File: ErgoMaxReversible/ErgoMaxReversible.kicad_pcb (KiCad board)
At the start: 2 copper layers, 182.8 x 169.2 mm, 104 parts, among them J1 PJ-320A, K1 KEYSW, K10 KEYSW, K11 KEYSW, K12 KEYSW, K13 KEYSW, K14 KEYSW, K15 KEYSW, K16 KEYSW, K17 KEYSW, K18 KEYSW, K19 KEYSW, K2 KEYSW, K20 KEYSW, K21 KEYSW, K22 KEYSW, K23 KEYSW, K24 KEYSW, K25 KEYSW, K26 KEYSW, K27 KEYSW, K28 KEYSW, K29 KEYSW, K3 KEYSW, K30 KEYSW, K31 KEYSW, K32 KEYSW, K33 KEYSW, K34 KEYSW, K35 KEYSW, K36 KEYSW, K37 KEYSW, K38 KEYSW, K39 KEYSW, K4 KEYSW, K40 KEYSW, K41 KEYSW, K42 KEYSW, K43 KEYSW, K44 KEYSW, K5 KEYSW, K6 KEYSW, K7 KEYSW, K8 KEYSW, K9 KEYSW, U1 ProMicro

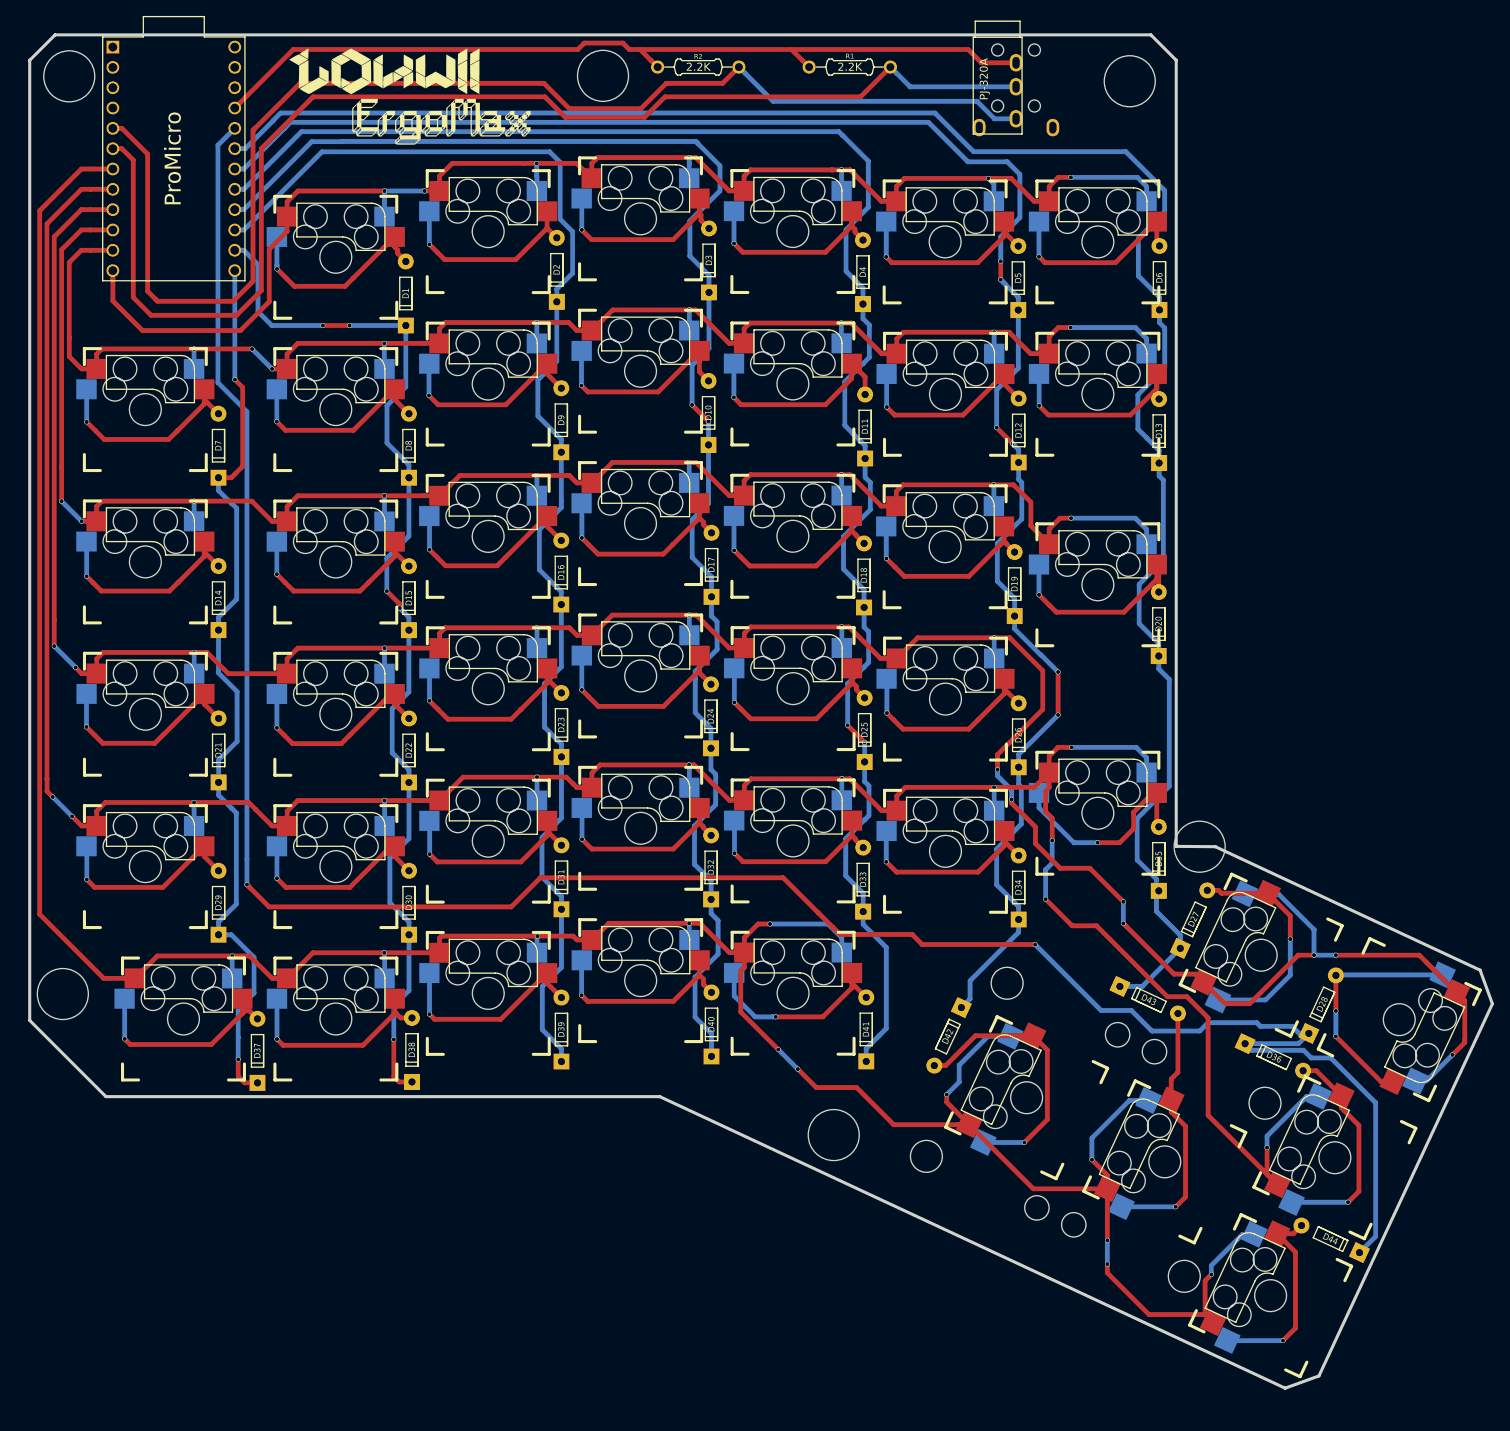
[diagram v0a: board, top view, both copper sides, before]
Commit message: improve footprints on reversible PCB and add sides markings
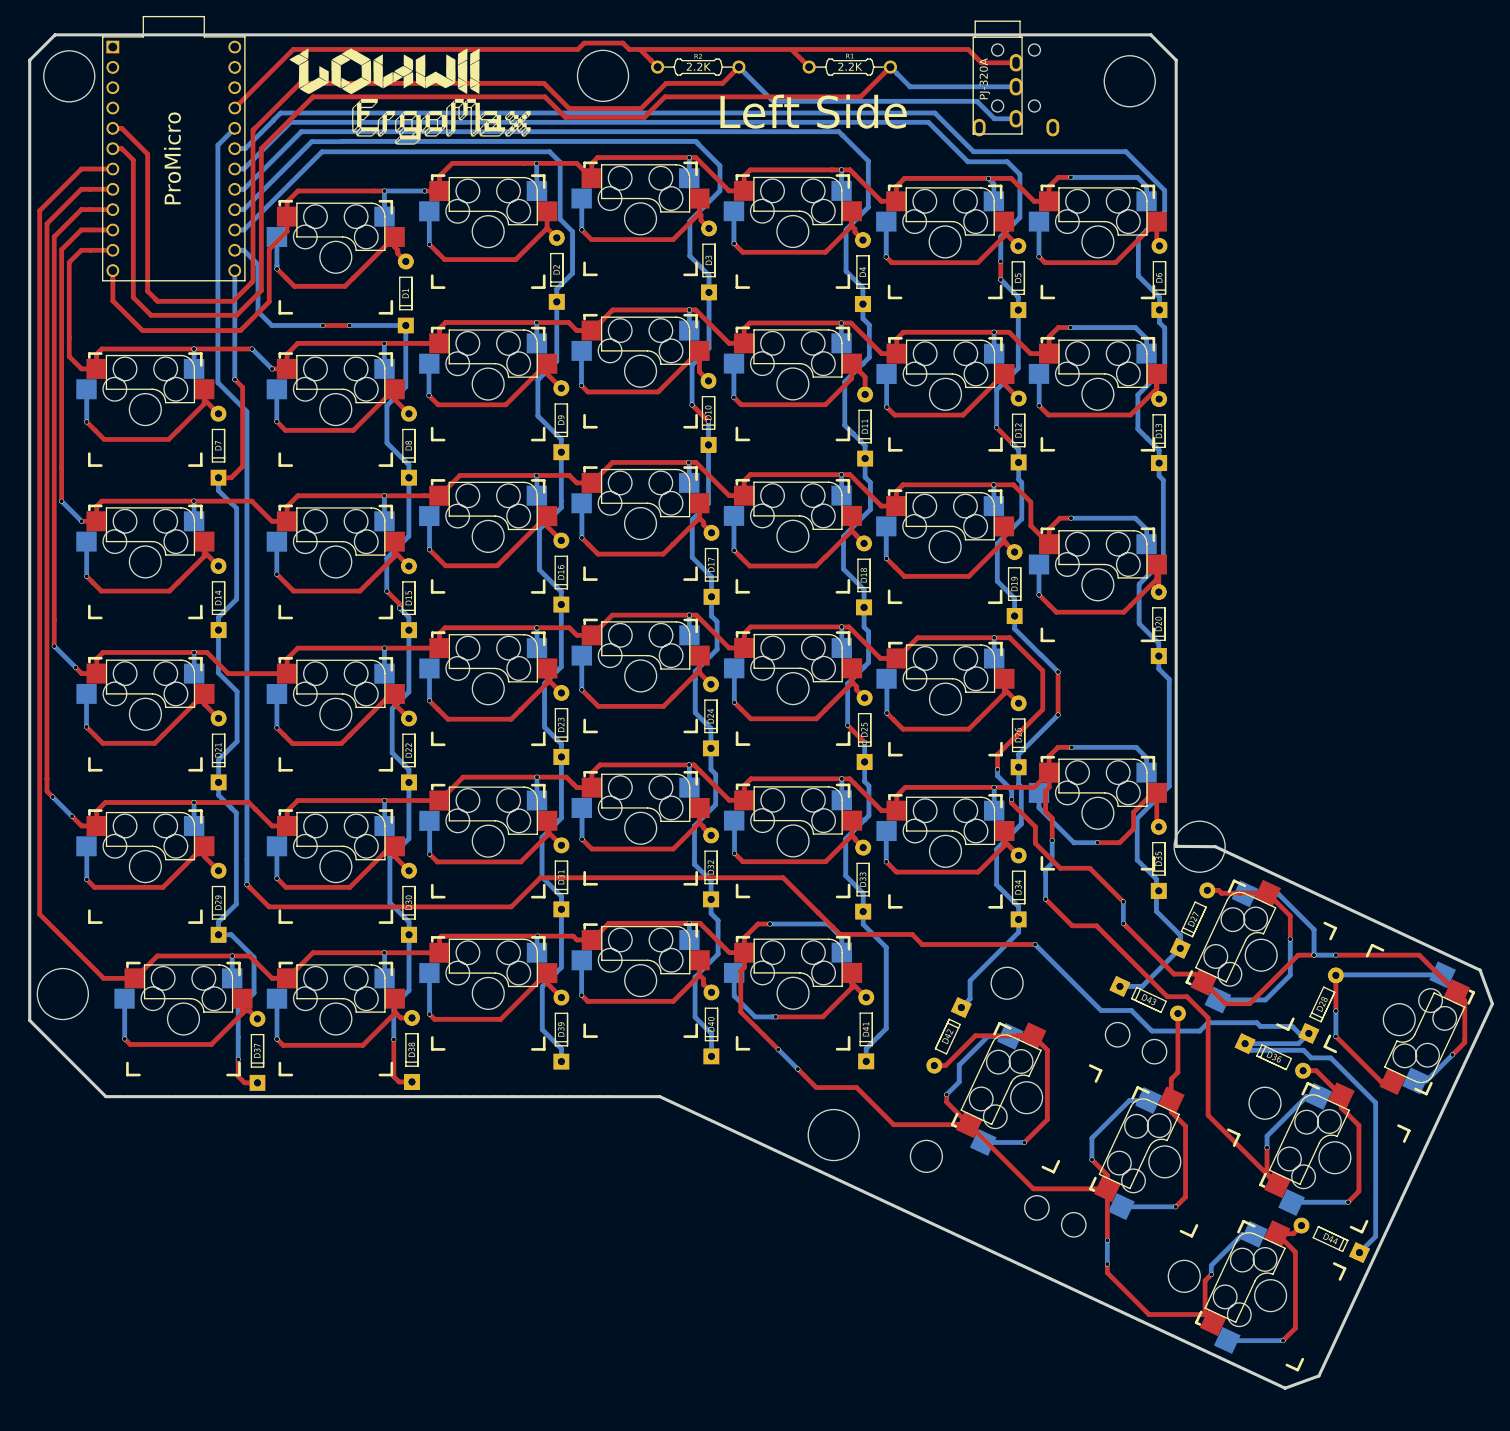
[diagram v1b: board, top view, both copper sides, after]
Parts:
- added Lg5: Logo, ErgoMax:LeftSideText, F.Cu at (208.2, 45.7)
- added Lg6: Logo, ErgoMax:RightSideText, F.Cu at (208.2, 45.7)
- K1, K10, K11, K12, K13, K14, K15, K16, K17, K18, K19, K2, K20, K21, K22, K23, K24, K25, K26, K27, K28, K29, K3, K30, K31, K32, K33, K34, K35, K36, K37, K38, K39, K4, K40, K41, K42, K43, K44, K5, K6, K7, K8, K9: footprint keyboard_parts:Kailh_MX_Socket_reversible -> ErgoMax:Kailh_MX_Socket_reversible

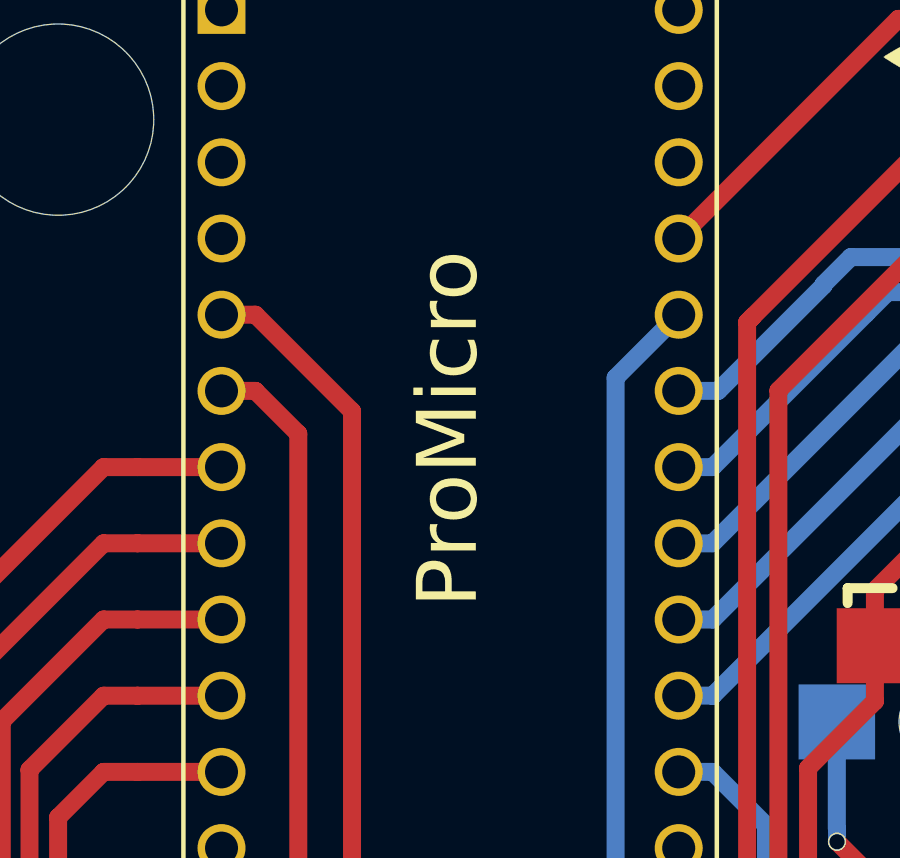
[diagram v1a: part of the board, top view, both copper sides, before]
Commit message: add readme for reversible PCB
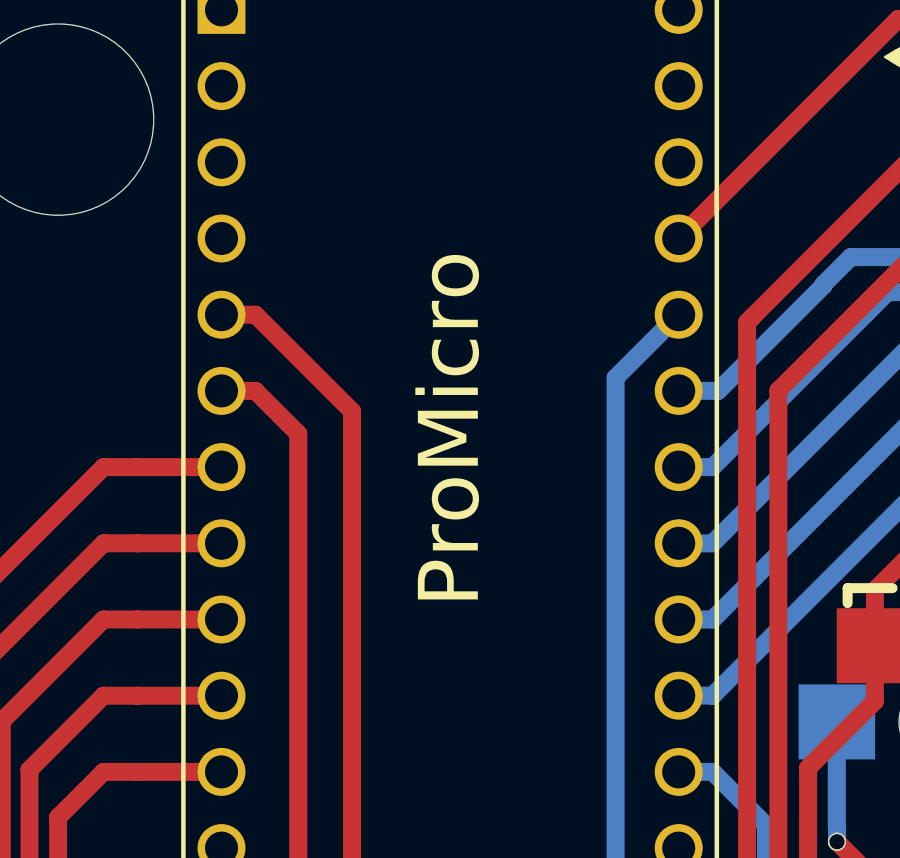
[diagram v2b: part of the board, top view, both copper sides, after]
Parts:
- U1: footprint promicro:ProMicro -> ErgoMax:ProMicroReversible

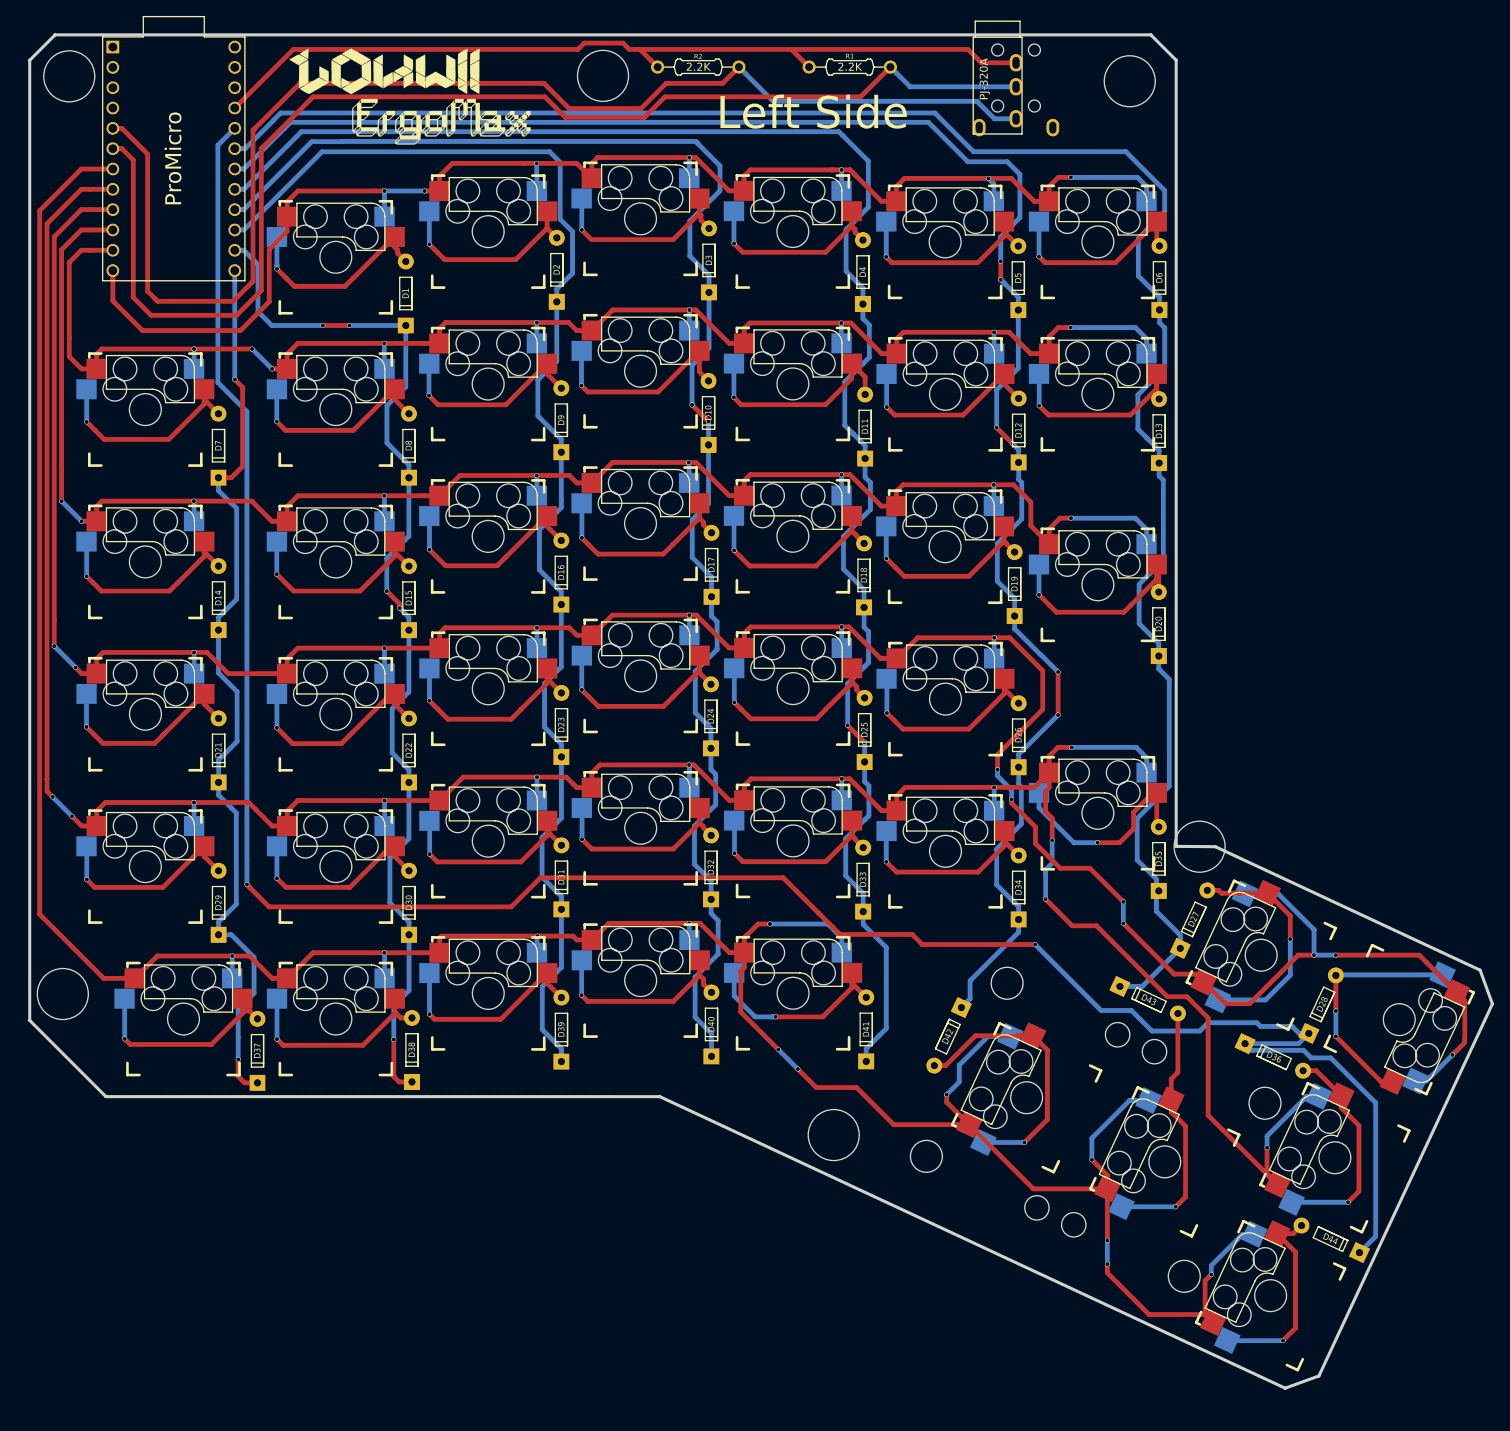
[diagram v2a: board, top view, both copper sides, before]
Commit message: Fix ground plane on reversible PCB
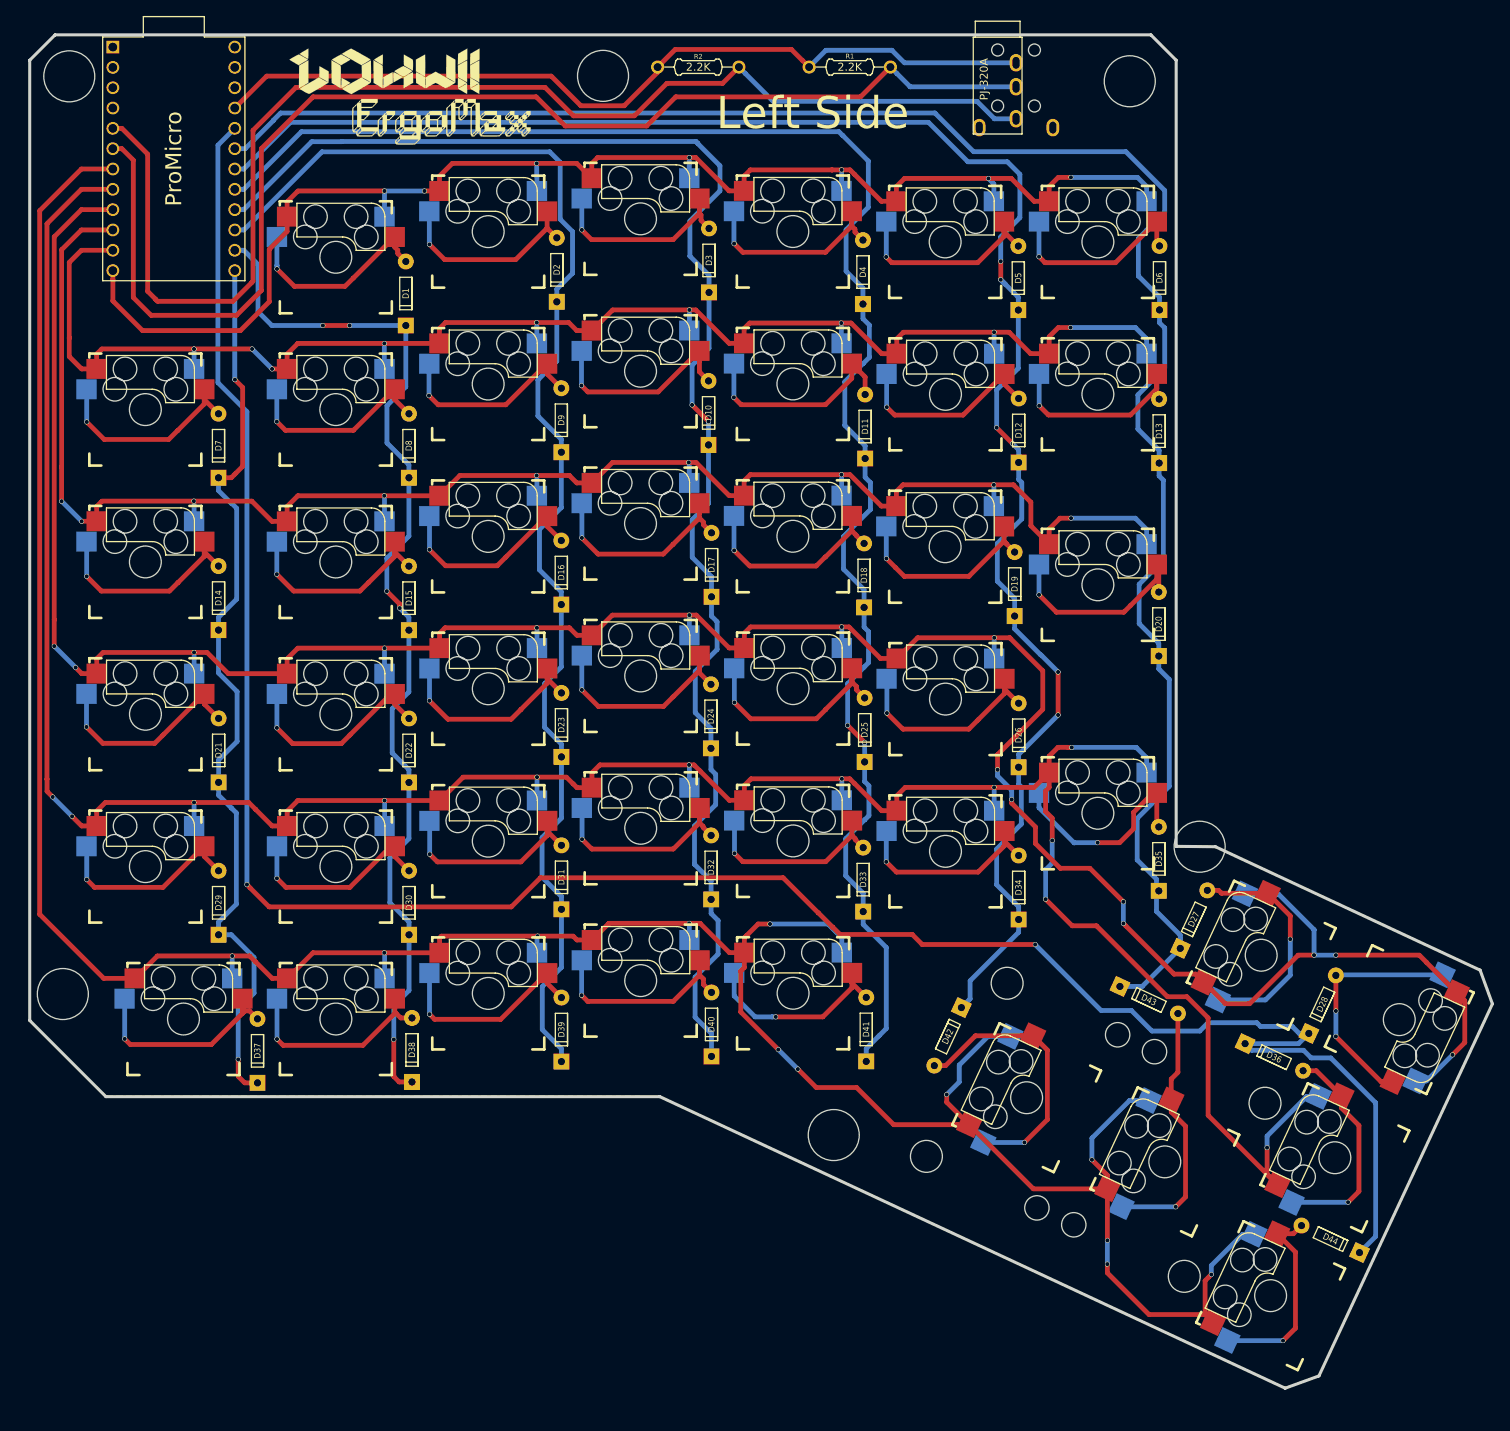
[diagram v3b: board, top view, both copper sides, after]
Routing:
- net Net-(D3-Pad2): track 28.0 -> 26.0 mm
- net Net-(D42-Pad2): track 36.2 -> 34.3 mm
- net Net-(D4-Pad2): track 27.9 -> 26.0 mm
- net VCC: track 108.3 -> 106.6 mm
- net Net-(D36-Pad2): track 29.0 -> 27.9 mm
- net SCL: track 158.0 -> 158.9 mm
- net Net-(D44-Pad2): track 26.3 -> 25.4 mm
- net /Col7: track 289.2 -> 288.7 mm
- net /Col6: track 239.1 -> 238.5 mm
- net Net-(D38-Pad2): track 26.5 -> 26.0 mm
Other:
- net class Default removed
